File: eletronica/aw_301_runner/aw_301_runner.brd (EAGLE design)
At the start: 44.1 x 53.3 mm, 9 parts, among them IC1 ATTINY2313V, Q1 4 Mhz

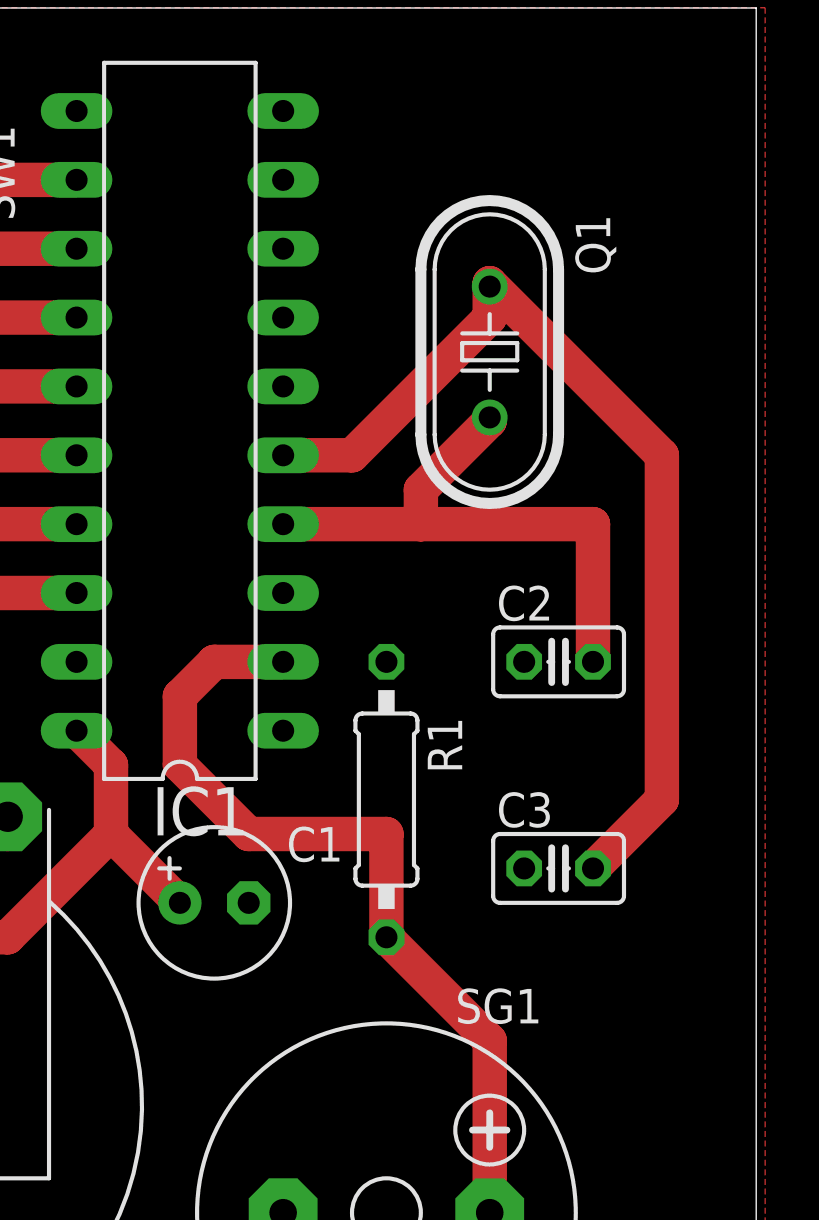
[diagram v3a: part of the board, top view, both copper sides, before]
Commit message: 
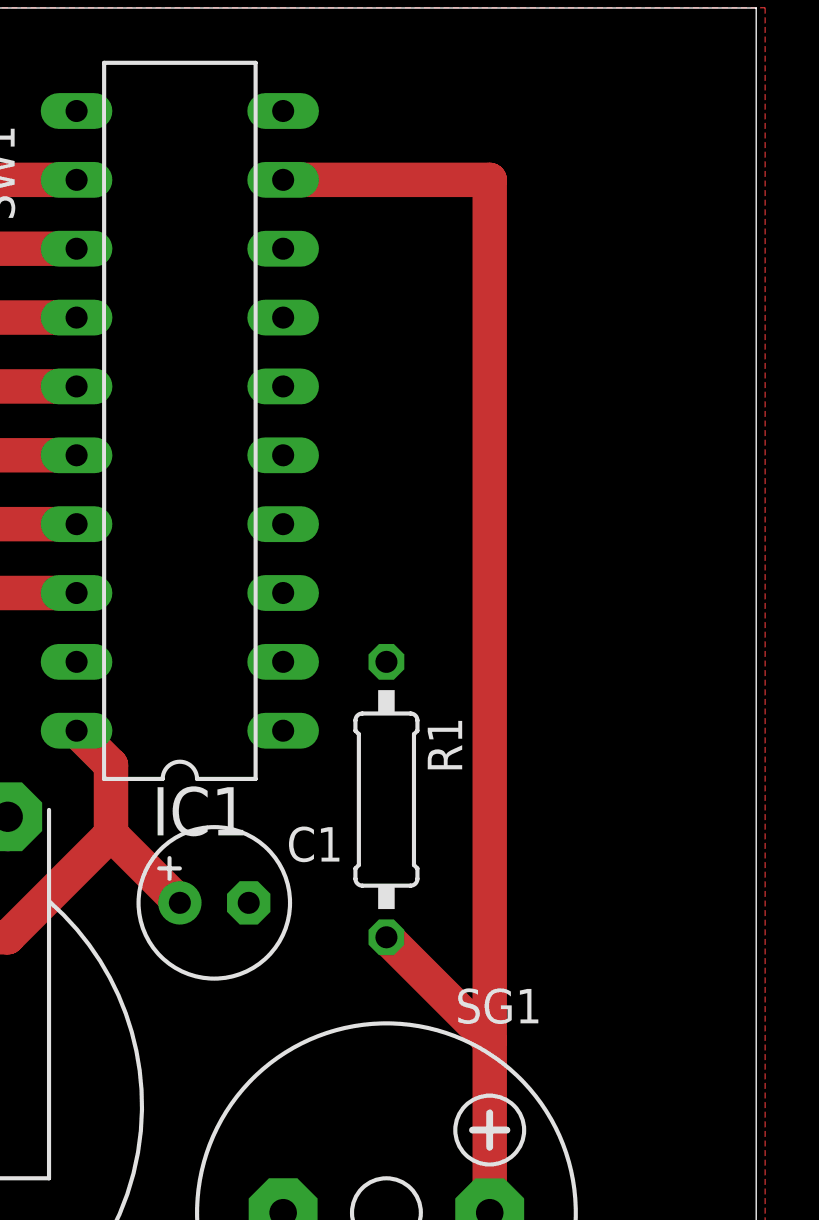
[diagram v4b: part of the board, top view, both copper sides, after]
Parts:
- removed C2, C3: 22pF, rcl:C025-025X050
- removed Q1: 4 Mhz, crystal:HC49U70
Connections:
- removed net N$2: C2.2, IC1.4, Q1.2
- removed net N$3: C3.2, IC1.5, Q1.1
- removed net N$6: IC1.2, R1.2, SG1.+
- new net N$4: IC1.9, R1.2, SG1.+
- net GND: no longer C2.1, C3.1
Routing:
- net N$4: track 0.00 -> 51.1 mm
- net N$3: track 36.3 -> 0.00 mm
- net N$6: track 31.1 -> 0.00 mm
- net N$2: track 21.5 -> 0.00 mm
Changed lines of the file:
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@@
 </element>
 <element name="C1" library="resistor" package="E2,5-6" value="100mF" x="24.13" y="46.99"/>
-<element name="Q1" library="crystal" package="HC49U70" value="4 Mhz" x="34.29" y="67.31" rot="R270">
-<attribute name="OC_NEWARK" value="unknown" x="34.29" y="67.31" size="1.778" layer="27" rot="R270" display="off"/>
-<attribute name="MPN" value="" x="34.29" y="67.31" size="1.778" layer="27" rot="R270" display="off"/>
-<attribute name="MF" value="" x="34.29" y="67.31" size="1.778" layer="27" rot="R270" display="off"/>
-<attribute name="OC_FARNELL" value="unknown" x="34.29" y="67.31" size="1.778" layer="27" rot="R270" display="off"/>
-</element>
-<element name="C2" library="rcl" package="C025-025X050" value="22pF" x="36.83" y="55.88"/>
-<element name="C3" library="rcl" package="C025-025X050" value="22pF" x="36.83" y="48.26"/>
 <element name="R1" library="rcl" package="0207/10" value="1M" x="30.48" y="50.8" rot="R270"/>
 </elements>
 <signals>
-<signal name="N$2">
-<contactref element="IC1" pad="4"/>
-<contactref element="Q1" pad="2"/>
-<contactref element="C2" pad="2"/>
-<wire x1="38.1" y1="60.96" x2="31.75" y2="60.96" width="1.27" layer="1"/>
-<wire x1="31.75" y1="60.96" x2="26.67" y2="60.96" width="1.27" layer="1"/>
-<wire x1="38.1" y1="55.88" x2="38.1" y2="60.96" width="1.27" layer="1"/>
-<wire x1="31.75" y1="62.23" x2="34.29" y2="64.77" width="1.27" layer="1"/>
-<wire x1="31.75" y1="60.96" x2="31.75" y2="62.23" width="1.27" layer="1"/>
-<wire x1="34.29" y1="64.77" x2="34.29" y2="64.897" width="1.27" layer="1"/>
-</signal>
-<signal name="N$3">
-<contactref element="IC1" pad="5"/>
-<contactref element="Q1" pad="1"/>
-<contactref element="C3" pad="2"/>
-<wire x1="40.64" y1="50.8" x2="38.1" y2="48.26" width="1.27" layer="1"/>
-<wire x1="40.64" y1="63.5" x2="40.64" y2="50.8" width="1.27" layer="1"/>
-<wire x1="34.29" y1="69.85" x2="40.64" y2="63.5" width="1.27" layer="1"/>
-<wire x1="29.21" y1="63.5" x2="26.67" y2="63.5" width="1.27" layer="1"/>
-<wire x1="34.29" y1="68.58" x2="29.21" y2="63.5" width="1.27" layer="1"/>
-<wire x1="34.29" y1="69.723" x2="34.29" y2="68.58" width="1.27" layer="1"/>
-<wire x1="34.29" y1="69.85" x2="34.29" y2="69.723" width="1.27" layer="1"/>
-</signal>
 <signal name="VCC">
 <contactref element="SW1" pad="8"/>
@@
 <wire x1="6.35" y1="55.88" x2="11.43" y2="50.8" width="1.27" layer="1"/>
 </signal>
-<signal name="N$6">
-<contactref element="IC1" pad="2"/>
-<contactref element="SG1" pad="+"/>
-<contactref element="R1" pad="2"/>
-<wire x1="34.29" y1="41.91" x2="30.48" y2="45.72" width="1.27" layer="1"/>
-<wire x1="34.29" y1="35.56" x2="34.29" y2="41.91" width="1.27" layer="1"/>
-<wire x1="24.13" y1="55.88" x2="26.67" y2="55.88" width="1.27" layer="1"/>
-<wire x1="22.86" y1="54.61" x2="24.13" y2="55.88" width="1.27" layer="1"/>
-<wire x1="22.86" y1="52.07" x2="22.86" y2="54.61" width="1.27" layer="1"/>
-<wire x1="25.4" y1="49.53" x2="22.86" y2="52.07" width="1.27" layer="1"/>
-<wire x1="30.48" y1="49.53" x2="25.4" y2="49.53" width="1.27" layer="1"/>
-<wire x1="30.48" y1="45.72" x2="30.48" y2="49.53" width="1.27" layer="1"/>
-</signal>
 <signal name="GND">
 <contactref element="IC1" pad="1"/>
 <contactref element="IC1" pad="10"/>
 <contactref element="G1" pad="-"/>
-<contactref element="SG1" pad="-"/>
 <contactref element="C1" pad="-"/>
-<contactref element="C2" pad="1"/>
-<contactref element="C3" pad="1"/>
-<contactref element="R1" pad="1"/>
 <polygon width="0.4064" layer="1">
 <vertex x="0" y="80.01"/>
@@
 <vertex x="0" y="26.67"/>
 </polygon>
+<contactref element="R1" pad="1"/>
+<contactref element="SG1" pad="-"/>
 </signal>
 <signal name="N$8">
@@
 <wire x1="16.51" y1="49.53" x2="16.51" y2="50.165" width="1.27" layer="1"/>
 </signal>
+<signal name="N$4">
+<contactref element="R1" pad="2"/>
+<contactref element="IC1" pad="9"/>
+<contactref element="SG1" pad="+"/>
+<wire x1="34.29" y1="41.91" x2="30.48" y2="45.72" width="1.27" layer="1"/>
+<wire x1="34.29" y1="35.56" x2="34.29" y2="41.91" width="1.27" layer="1"/>
+<wire x1="34.29" y1="73.66" x2="26.67" y2="73.66" width="1.27" layer="1"/>
+<wire x1="34.29" y1="41.91" x2="34.29" y2="73.66" width="1.27" layer="1"/>
+</signal>
 </signals>

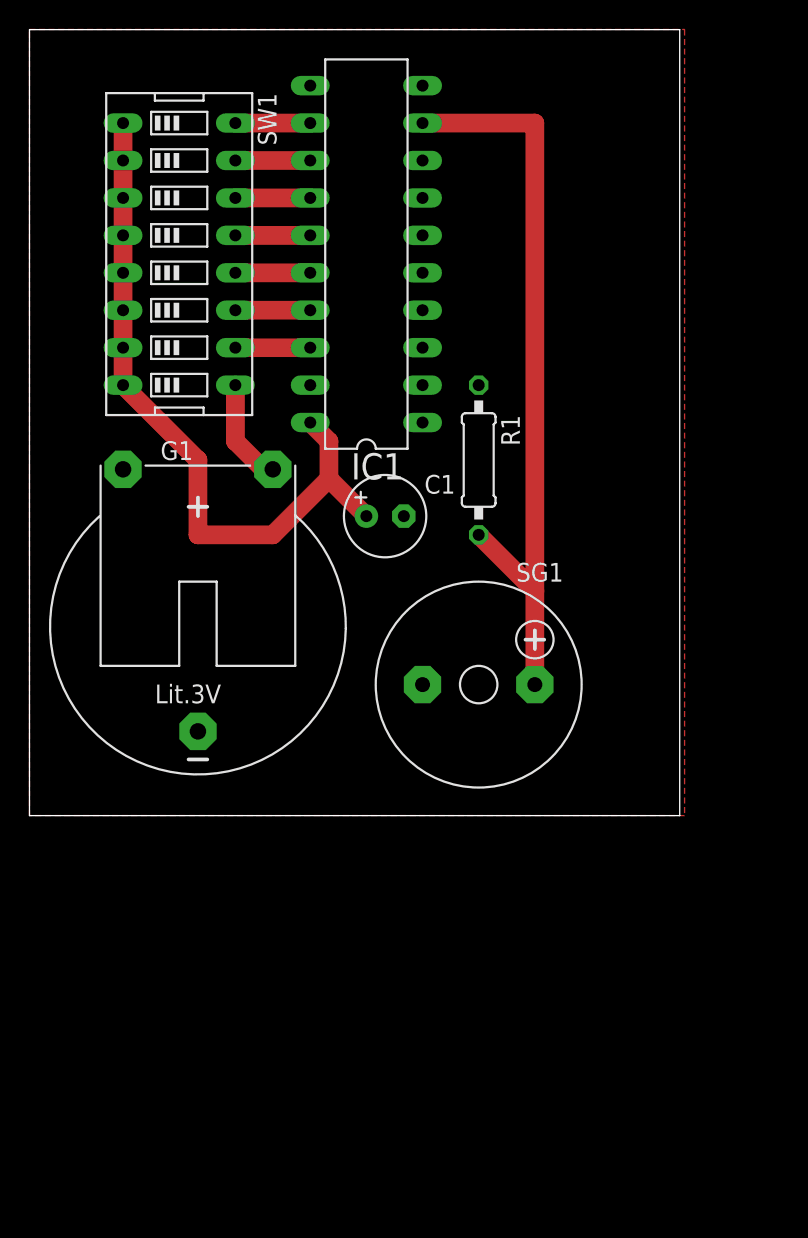
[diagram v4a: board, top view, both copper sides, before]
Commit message: 
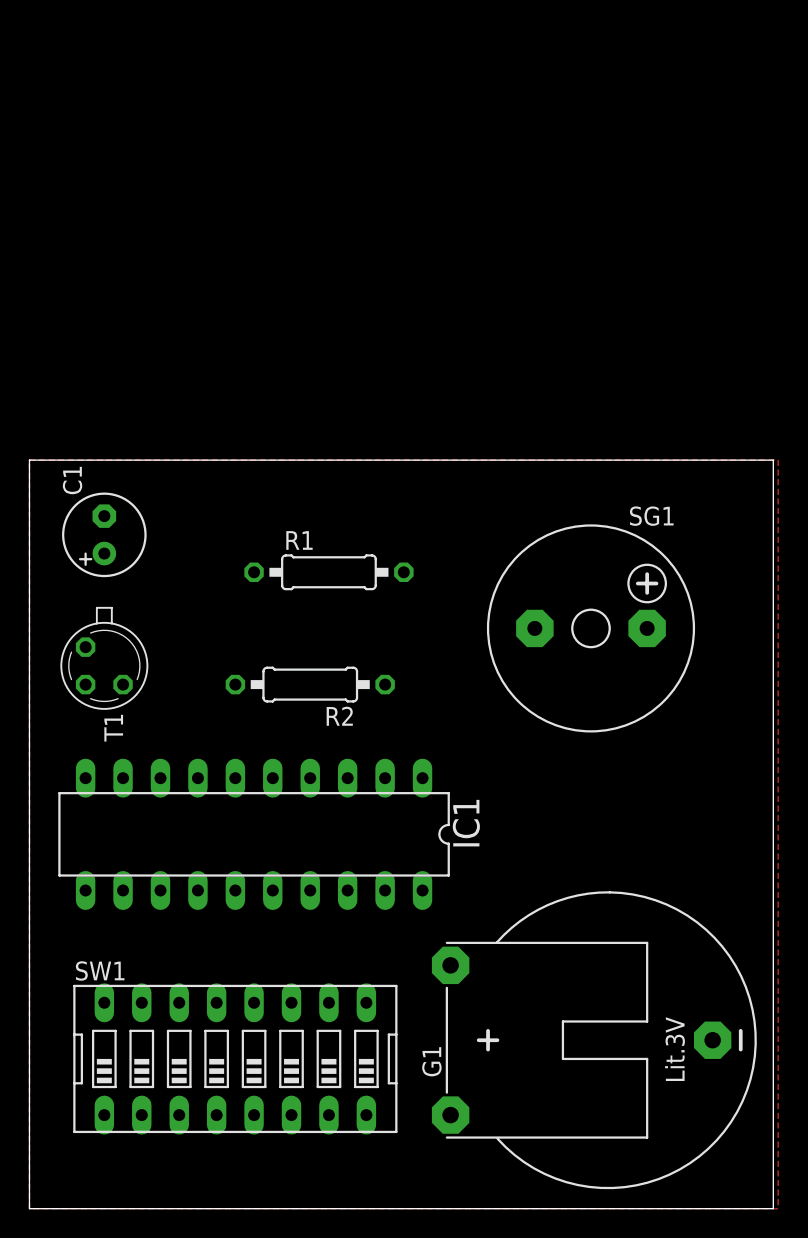
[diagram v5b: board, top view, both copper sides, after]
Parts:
- added R2: ?, rcl:0207/10
- added T1: 2N2222, transistor:TO18
- R1: value 1M -> ?
- moved SW1 54.7 mm to (14.0, 10.2), turned to 0 degrees
- moved IC1 40.1 mm to (15.2, 25.4), turned to 180 degrees
- moved G1 39.5 mm to (39.4, 11.4), turned to 90 degrees
- moved C1 19.1 mm to (5.08, 45.7), turned to 90 degrees
- moved R1 12.7 mm to (20.3, 43.2), turned to 0 degrees
- moved SG1 8.52 mm to (38.1, 39.4)
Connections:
- new net N$1: SW1.1, SW1.2, SW1.3, SW1.4, SW1.5, SW1.6, SW1.7, SW1.8
- new net N$2: IC1.9, R2.2
- new net N$3: R2.1, T1.2
- net GND: now also T1.1; no longer R1.1, SG1.-
- net N$4: now also SG1.-, T1.3; no longer IC1.9, SG1.+
- net VCC: now also R1.1, SG1.+; no longer SW1.1, SW1.2, SW1.3, SW1.4, SW1.5, SW1.6, SW1.7, SW1.8
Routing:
- net N$4: track 51.1 -> 0.00 mm
- net VCC: track 48.4 -> 0.00 mm
- net N$5: track 8.04 -> 0.00 mm
- net N$9: track 5.08 -> 0.00 mm
- net N$8: track 5.08 -> 0.00 mm
- net N$14: track 5.08 -> 0.00 mm
- net N$13: track 5.08 -> 0.00 mm
- net N$12: track 5.08 -> 0.00 mm
- net N$11: track 5.08 -> 0.00 mm
- net N$10: track 5.08 -> 0.00 mm
- added copper zone on layer 1, net N$6
- removed copper zone on layer 1, net GND
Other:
- board size 44.1 x 53.3 mm -> 50.5 x 50.8 mm
